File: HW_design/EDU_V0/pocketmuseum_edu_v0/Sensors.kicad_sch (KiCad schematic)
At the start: 23 parts, among them Q301 BSS138, Q302 BSS138, Q303 BSS138, U301 ICM-20948, U302 ICP20100, U303 BH1750FVI, U304 T3902

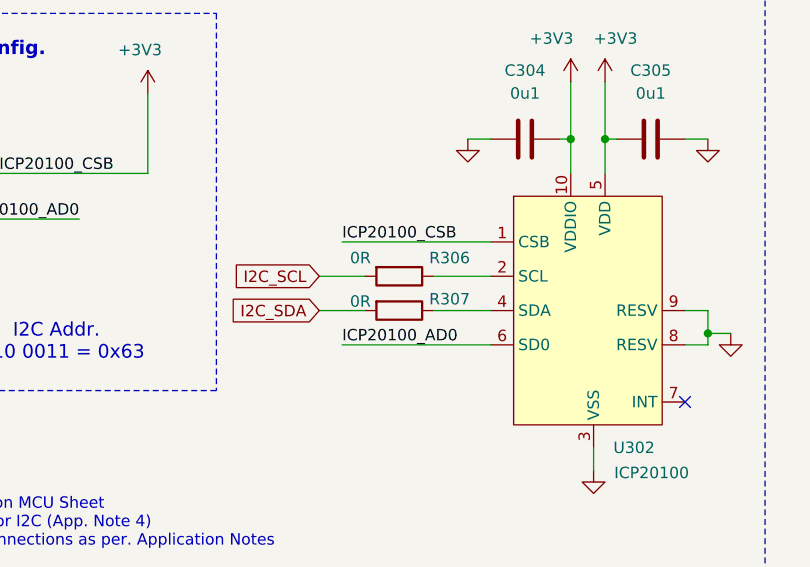
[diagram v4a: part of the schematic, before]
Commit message: EDUV0 added TP n routing in progress
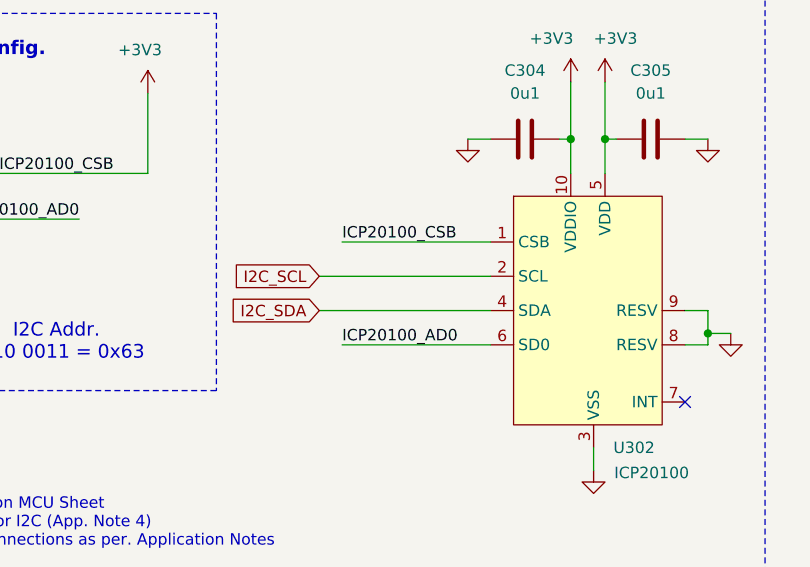
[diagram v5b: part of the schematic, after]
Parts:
- removed R306, R307: 0R, Resistor_SMD:R_0603_1608Metric, symbol Device:R
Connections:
- net I2C_SCL: now also U302.2 (SCL)
- net I2C_SDA: now also U302.4 (SDA)
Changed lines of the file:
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@@
 	(title_block
 		(title "POCKETMUSEUM EDU V0")
-		(date "2025-08-18")
-		(rev "2")
+		(date "2025-08-21")
+		(rev "3")
 		(company "Bucharest Applied STEAM Museum")
 		(comment 1 "Added MIC & LIGHT Sensor")
@@
 	(wire
 		(pts
-			(xy 189.23 59.69) (xy 195.58 59.69)
-		)
-		(stroke
-			(width 0)
-			(type default)
-		)
-	)
-	(wire
-		(pts
 			(xy 194.31 118.11) (xy 195.58 118.11)
 		)
@@
 	(wire
 		(pts
-			(xy 189.23 55.88) (xy 195.58 55.88)
-		)
-		(stroke
-			(width 0)
-			(type default)
-		)
-	)
-	(wire
-		(pts
 			(xy 208.28 34.29) (xy 208.28 40.64)
 		)
@@
 	(wire
 		(pts
-			(xy 176.53 59.69) (xy 181.61 59.69)
+			(xy 176.53 59.69) (xy 195.58 59.69)
 		)
 		(stroke
@@
 	(wire
 		(pts
-			(xy 176.53 55.88) (xy 181.61 55.88)
+			(xy 176.53 55.88) (xy 195.58 55.88)
 		)
 		(stroke
@@
 	)
 	(symbol
-		(lib_id "Device:R")
-		(at 185.42 59.69 270)
-		(unit 1)
-		(exclude_from_sim no)
-		(in_bom yes)
-		(on_board yes)
-		(dnp no)
-		(property "Reference" "R307"
-			(at 191.008 58.42 90)
-			(effects
-				(font
-					(size 1.27 1.27)
-				)
-			)
-		)
-		(property "Value" "0R"
-			(at 181.102 58.674 90)
-			(effects
-				(font
-					(size 1.27 1.27)
-				)
-			)
-		)
-		(property "Footprint" "Resistor_SMD:R_0603_1608Metric"
-			(at 185.42 57.912 90)
-			(effects
-				(font
-					(size 1.27 1.27)
-				)
-				(hide yes)
-			)
-		)
-		(property "Datasheet" "~"
-			(at 185.42 59.69 0)
-			(effects
-				(font
-					(size 1.27 1.27)
-				)
-				(hide yes)
-			)
-		)
-		(property "Description" "Resistor"
-			(at 185.42 59.69 0)
-			(effects
-				(font
-					(size 1.27 1.27)
-				)
-				(hide yes)
-			)
-		)
-		(property "JLCPCB Link" "https://jlcpcb.com/partdetail/16080-0603WAJ0000T5E/C15402"
-			(at 185.42 59.69 0)
-			(effects
-				(font
-					(size 1.27 1.27)
-				)
-				(hide yes)
-			)
-		)
-		(property "Manufacturer" "UNI-ROYAL(Uniroyal Elec) "
-			(at 185.42 59.69 0)
-			(effects
-				(font
-					(size 1.27 1.27)
-				)
-				(hide yes)
-			)
-		)
-		(property "Manufacturer P/N" "0603WAJ0000T5E"
-			(at 185.42 59.69 0)
-			(effects
-				(font
-					(size 1.27 1.27)
-				)
-				(hide yes)
-			)
-		)
-		(pin "2"
-		)
-		(pin "1"
-		)
-		(instances
-			(project "pocketmuseum_edu_v0"
-				(path "/4bede6f6-420d-49b9-8d53-bd69095749c2/36cdbd28-8810-4657-96de-41aba4386ff5"
-					(reference "R307")
-					(unit 1)
-				)
-			)
-		)
-	)
-	(symbol
 		(lib_id "power:GND")
 		(at 184.15 121.92 0)
@@
 					(unit 1)
 				)
-			)
-		)
-	)
-	(symbol
-		(lib_id "Device:R")
-		(at 185.42 55.88 270)
-		(unit 1)
-		(exclude_from_sim no)
-		(in_bom yes)
-		(on_board yes)
-		(dnp no)
-		(property "Reference" "R306"
-			(at 191.008 53.848 90)
-			(effects
-				(font
-					(size 1.27 1.27)
-				)
-			)
-		)
-		(property "Value" "0R"
-			(at 181.102 53.848 90)
-			(effects
-				(font
-					(size 1.27 1.27)
-				)
-			)
-		)
-		(property "Footprint" "Resistor_SMD:R_0603_1608Metric"
-			(at 185.42 54.102 90)
-			(effects
-				(font
-					(size 1.27 1.27)
-				)
-				(hide yes)
-			)
-		)
-		(property "Datasheet" "~"
-			(at 185.42 55.88 0)
-			(effects
-				(font
-					(size 1.27 1.27)
-				)
-				(hide yes)
-			)
-		)
-		(property "Description" "Resistor"
-			(at 185.42 55.88 0)
-			(effects
-				(font
-					(size 1.27 1.27)
-				)
-				(hide yes)
-			)
-		)
-		(property "JLCPCB Link" "https://jlcpcb.com/partdetail/16080-0603WAJ0000T5E/C15402"
-			(at 185.42 55.88 0)
-			(effects
-				(font
-					(size 1.27 1.27)
-				)
-				(hide yes)
-			)
-		)
-		(property "Manufacturer" "UNI-ROYAL(Uniroyal Elec) "
-			(at 185.42 55.88 0)
-			(effects
-				(font
-					(size 1.27 1.27)
-				)
-				(hide yes)
-			)
-		)
-		(property "Manufacturer P/N" "0603WAJ0000T5E"
-			(at 185.42 55.88 0)
-			(effects
-				(font
-					(size 1.27 1.27)
-				)
-				(hide yes)
-			)
-		)
-		(pin "2"
-		)
-		(pin "1"
-		)
-		(instances
-			(project "pocketmuseum_edu_v0"
-				(path "/4bede6f6-420d-49b9-8d53-bd69095749c2/36cdbd28-8810-4657-96de-41aba4386ff5"
-					(reference "R306")
-					(unit 1)
-				)
